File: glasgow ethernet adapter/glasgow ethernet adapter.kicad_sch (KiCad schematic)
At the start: 63 parts, among them J1 Glasgow Port, J2 RJ45_Amphenol_RJMG201K21120FR, U1 MxL86110, Y1 25 MHz

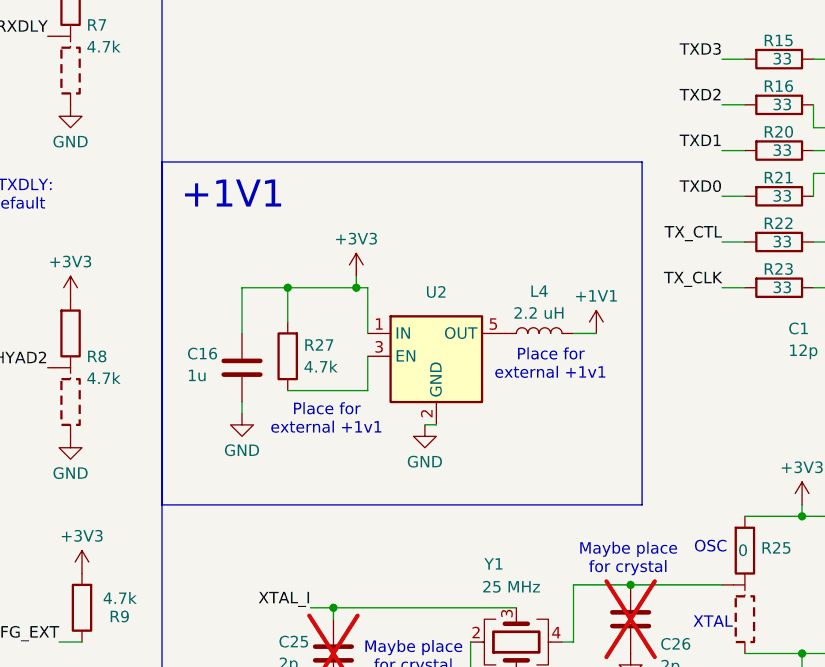
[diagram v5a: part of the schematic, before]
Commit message: add Cout to +1v1, add to resistor silk
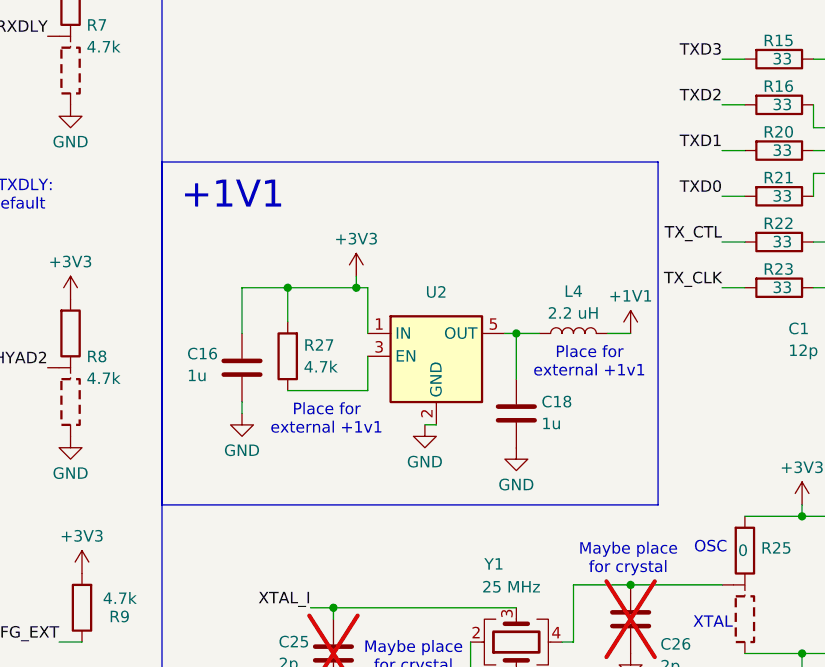
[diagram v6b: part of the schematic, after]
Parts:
- added C18: 1u, Capacitor_SMD:C_0603_1608Metric, symbol Device:C
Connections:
- net GND: now also C18.2
- net at L4.1, U2.5 (OUT): now also C18.1
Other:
- moved on the sheet: L4
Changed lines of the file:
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@@
 	)
 	(junction
+		(at 118.11 133.35)
+		(diameter 0)
+		(color 0 0 0 0)
+	)
+	(junction
 		(at 204.47 63.5)
 		(diameter 0)
@@
 	(wire
 		(pts
-			(xy 127 133.35) (xy 124.46 133.35)
+			(xy 130.81 133.35) (xy 128.27 133.35)
 		)
 		(stroke
@@
 	(wire
 		(pts
+			(xy 118.11 133.35) (xy 118.11 138.43)
+		)
+		(stroke
+			(width 0)
+			(type default)
+		)
+	)
+	(wire
+		(pts
 			(xy 40.64 54.61) (xy 38.1 54.61)
 		)
@@
 	(wire
 		(pts
+			(xy 118.11 133.35) (xy 116.84 133.35)
+		)
+		(stroke
+			(width 0)
+			(type default)
+		)
+	)
+	(wire
+		(pts
 			(xy 140.97 128.27) (xy 143.51 128.27)
 		)
@@
 	(wire
 		(pts
+			(xy 120.65 133.35) (xy 118.11 133.35)
+		)
+		(stroke
+			(width 0)
+			(type default)
+		)
+	)
+	(wire
+		(pts
 			(xy 219.71 91.44) (xy 222.25 91.44)
 		)
@@
 	(rectangle
 		(start 78.74 114.3)
-		(end 132.08 152.4)
+		(end 133.858 152.4)
 		(stroke
 			(width 0)
@@
 	(text "Place for \nexternal +1v1"
 		(exclude_from_sim no)
-		(at 121.92 136.906 0)
+		(at 126.238 136.652 0)
 		(effects
 			(font
@@
 	(symbol
 		(lib_id "power:+1V1")
-		(at 127 133.35 0)
+		(at 130.81 133.35 0)
 		(unit 1)
 		(exclude_from_sim no)
@@
 		(fields_autoplaced yes)
 		(property "Reference" "#PWR013"
-			(at 127 137.16 0)
+			(at 130.81 137.16 0)
 			(effects
 				(font
@@
 		)
 		(property "Value" "+1V1"
-			(at 127 129.2169 0)
+			(at 130.81 129.2169 0)
 			(effects
 				(font
@@
 		)
 		(property "Footprint" ""
-			(at 127 133.35 0)
+			(at 130.81 133.35 0)
 			(effects
 				(font
@@
 		)
 		(property "Datasheet" ""
-			(at 127 133.35 0)
+			(at 130.81 133.35 0)
 			(effects
 				(font
@@
 		)
 		(property "Description" "Power symbol creates a global label with name \"+1V1\""
-			(at 127 133.35 0)
+			(at 130.81 133.35 0)
 			(effects
 				(font
@@
 	)
 	(symbol
+		(lib_id "power:GND")
+		(at 118.11 146.05 0)
+		(unit 1)
+		(exclude_from_sim no)
+		(in_bom yes)
+		(on_board yes)
+		(dnp no)
+		(property "Reference" "#PWR059"
+			(at 118.11 152.4 0)
+			(effects
+				(font
+					(size 1.27 1.27)
+				)
+				(hide yes)
+			)
+		)
+		(property "Value" "GND"
+			(at 118.11 150.1831 0)
+			(effects
+				(font
+					(size 1.27 1.27)
+				)
+			)
+		)
+		(property "Footprint" ""
+			(at 118.11 146.05 0)
+			(effects
+				(font
+					(size 1.27 1.27)
+				)
+				(hide yes)
+			)
+		)
+		(property "Datasheet" ""
+			(at 118.11 146.05 0)
+			(effects
+				(font
+					(size 1.27 1.27)
+				)
+				(hide yes)
+			)
+		)
+		(property "Description" "Power symbol creates a global label with name \"GND\" , ground"
+			(at 118.11 146.05 0)
+			(effects
+				(font
+					(size 1.27 1.27)
+				)
+				(hide yes)
+			)
+		)
+		(pin "1"
+		)
+		(instances
+			(project "glasgow ethernet adapter"
+				(path "/fb29a680-9889-4434-a9c5-c40bcbb39141"
+					(reference "#PWR059")
+					(unit 1)
+				)
+			)
+		)
+	)
+	(symbol
 		(lib_id "power:+3V3")
 		(at 166.37 128.27 90)
@@
 	(symbol
 		(lib_id "Device:L")
-		(at 120.65 133.35 90)
+		(at 124.46 133.35 90)
 		(unit 1)
 		(exclude_from_sim no)
@@
 		(dnp no)
 		(property "Reference" "L4"
-			(at 120.65 128.7002 90)
+			(at 124.46 128.7002 90)
 			(effects
 				(font
@@
 		)
 		(property "Value" "2.2 uH"
-			(at 120.65 131.1245 90)
+			(at 124.46 131.1245 90)
 			(effects
 				(font
@@
 		)
 		(property "Footprint" "Inductor_SMD:L_0603_1608Metric"
-			(at 120.65 133.35 0)
+			(at 124.46 133.35 0)
 			(effects
 				(font
@@
 		)
 		(property "Datasheet" "~"
-			(at 120.65 133.35 0)
+			(at 124.46 133.35 0)
 			(effects
 				(font
@@
 		)
 		(property "Description" "Inductor"
-			(at 120.65 133.35 0)
+			(at 124.46 133.35 0)
 			(effects
 				(font
@@
 					(unit 1)
 				)
+			)
+		)
+	)
+	(symbol
+		(lib_id "Device:C")
+		(at 118.11 142.24 0)
+		(unit 1)
+		(exclude_from_sim no)
+		(in_bom yes)
+		(on_board yes)
+		(dnp no)
+		(property "Reference" "C18"
+			(at 120.904 140.97 0)
+			(effects
+				(font
+					(size 1.27 1.27)
+				)
+				(justify left)
+			)
+		)
+		(property "Value" "1u"
+			(at 120.904 143.3943 0)
+			(effects
+				(font
+					(size 1.27 1.27)
+				)
+				(justify left)
+			)
+		)
+		(property "Footprint" "Capacitor_SMD:C_0603_1608Metric"
+			(at 119.0752 146.05 0)
+			(effects
+				(font
+					(size 1.27 1.27)
+				)
+				(hide yes)
+			)
+		)
+		(property "Datasheet" "~"
+			(at 118.11 142.24 0)
+			(effects
+				(font
+					(size 1.27 1.27)
+				)
+				(hide yes)
+			)
+		)
+		(property "Description" "Unpolarized capacitor"
+			(at 118.11 142.24 0)
+			(effects
+				(font
+					(size 1.27 1.27)
+				)
+				(hide yes)
+			)
+		)
+		(pin "2"
+		)
+		(pin "1"
+		)
+		(instances
+			(project "glasgow ethernet adapter"
+				(path "/fb29a680-9889-4434-a9c5-c40bcbb39141"
+					(reference "C18")
+					(unit 1)
+				)

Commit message: add JLC part numbers
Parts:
- C1, C2: JLC Part ID (none) -> C1547
- C10, C11, C14, C15, C17, C20: JLC Part ID (none) -> C29823
- C12, C13, C19, C22, C27, C28, C3, C5, C6, C7, C8, C9: JLC Part ID (none) -> C967572
- C16, C18: JLC Part ID (none) -> C1592
- C4: JLC Part ID (none) -> C1525
- J1: JLC Part ID (none) -> C124419
- J2: JLC Part ID (none) -> C3179446
- L1, L2, L3, L4: JLC Part ID (none) -> C17305
- R1, R11, R2, R27, R3, R4, R5, R6, R7, R8, R9: JLC Part ID (none) -> C25900
- R10, R13, R24, R25, R26: JLC Part ID (none) -> C17168
- R12: JLC Part ID (none) -> C102924
- R14: JLC Part ID (none) -> C21189
- R15, R16, R20, R21, R22, R23: JLC Part ID (none) -> C25105
- R17, R18, R19: JLC Part ID (none) -> C173697
- U1: JLC Part ID (none) -> C187932
- Y1: JLC Part ID (none) -> C669080

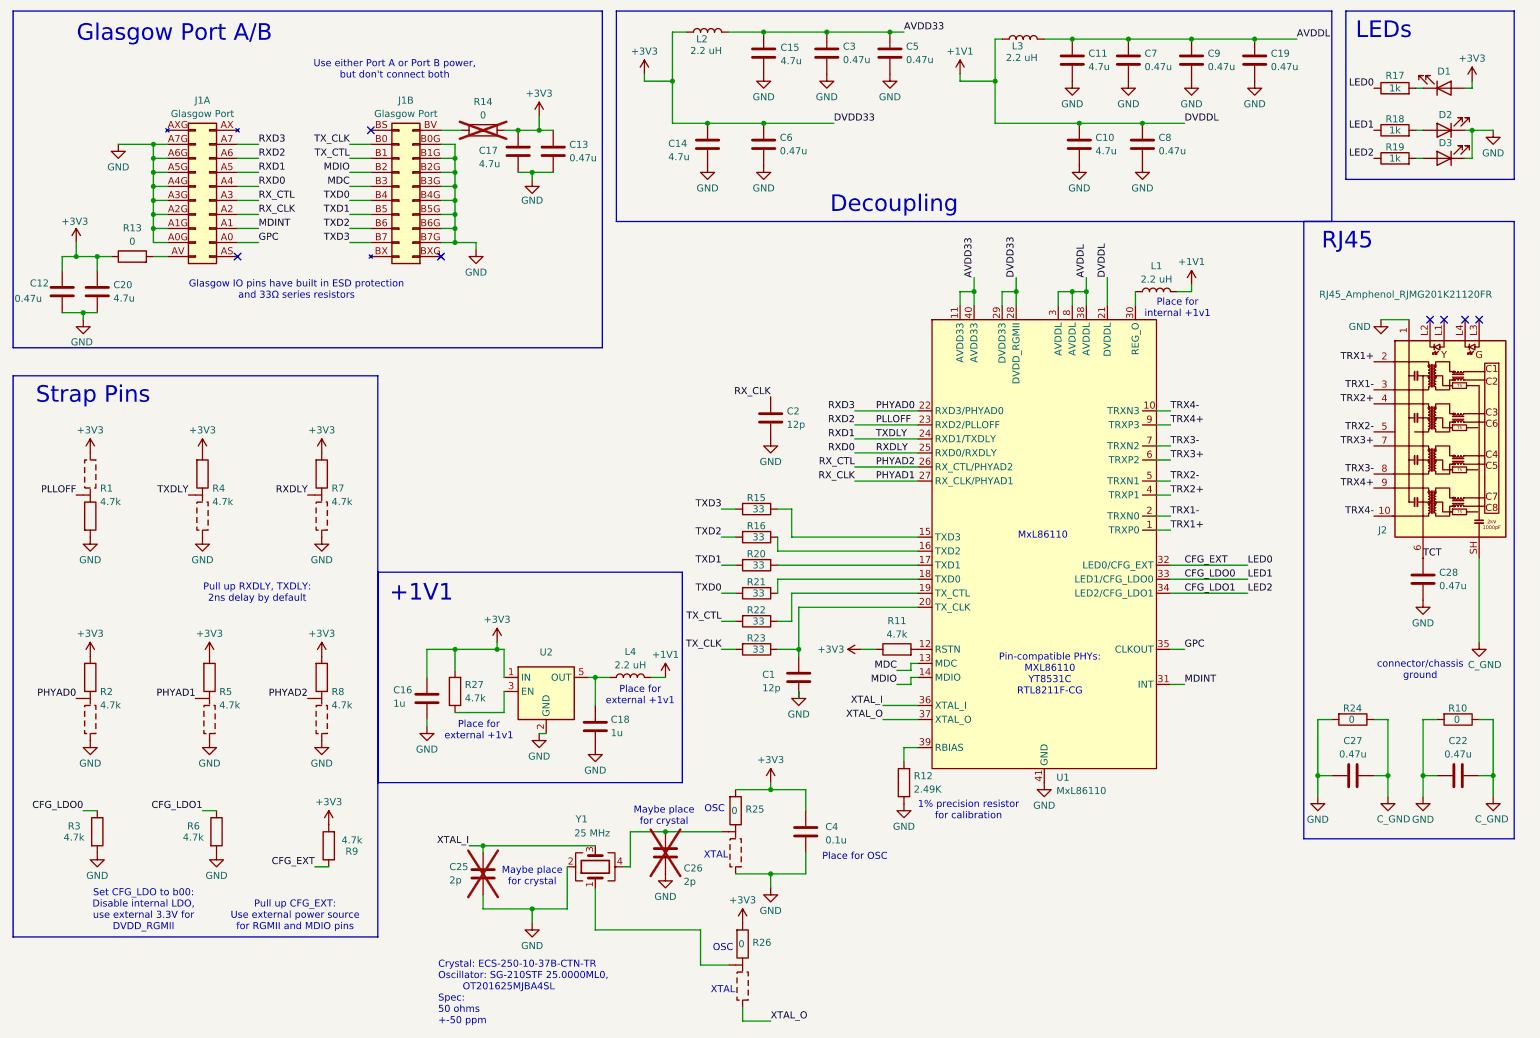
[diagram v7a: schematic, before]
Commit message: replace LDO with one from JLC, renumber schematic
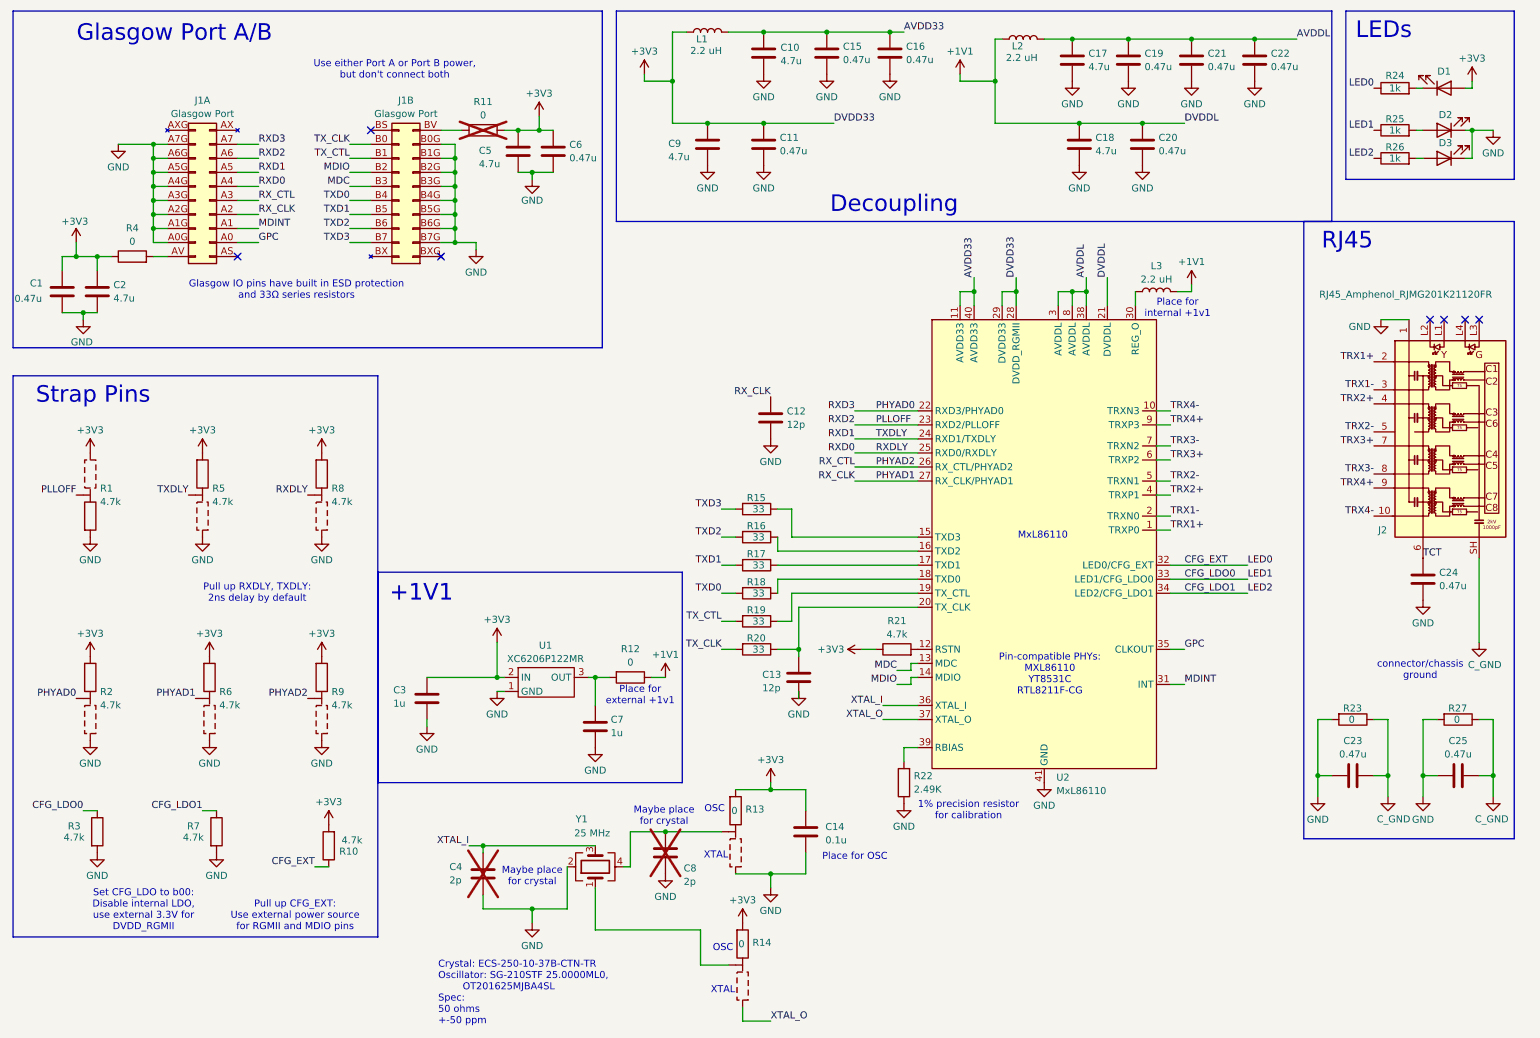
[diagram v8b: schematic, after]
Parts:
- removed L4: 2.2 uH, Inductor_SMD:L_0603_1608Metric, symbol Device:L
- removed R27: 4.7k, Resistor_SMD:R_0402_1005Metric, symbol Device:R
- removed U2: ~, Package_TO_SOT_SMD:SOT-23-5, symbol glasgow:TLV74311PDBVR
- added R12: 0, Resistor_SMD:R_0603_1608Metric, symbol Device:R
- added U1: XC6206P122MR, Package_TO_SOT_SMD:SOT-23, symbol glasgow:XC6206P122MR
- renumbered C12 to C1, C15 to C10, C6 to C11, C2 to C12, C1 to C13, C4 to C14, C3 to C15, C5 to C16, C11 to C17, C10 to C18, C7 to C19, C20 to C2, C8 to C20, C9 to C21, C19 to C22, C27 to C23, C28 to C24, C22 to C25, C16 to C3, C25 to C4, C17 to C5, C13 to C6, C18 to C7, C26 to C8, C14 to C9, L2 to L1, L3 to L2, L1 to L3, R9 to R10, R14 to R11, R25 to R13, R26 to R14, R20 to R17, R21 to R18, R22 to R19, R23 to R20, R11 to R21, R12 to R22, R24 to R23, R17 to R24, R18 to R25, R19 to R26, R10 to R27, R13 to R4, R4 to R5, R5 to R6, R6 to R7, R7 to R8, R8 to R9, U1 to U2
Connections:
- net +1V1: now also R12.1
- net +3V3: now also U1.2 (IN)
- net GND: now also U1.1 (GND)
- net at C7.1: now also R12.2, U1.3 (OUT)
